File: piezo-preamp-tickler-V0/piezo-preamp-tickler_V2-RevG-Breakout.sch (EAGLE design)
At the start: 67 parts, among them IC1 OPA2134UA, Q1 J201SOT-23, Q2 J201SOT-23, SW2-SPST INPUT-select

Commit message: updated footprints
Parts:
- removed C14: 68uF, SparkFun:CAP_POL3528
- removed SC4503: VREG12_SOT23-5, CMU-ArtFab:VREG12_SOT23-5
- added C11: 10uF, adafruit:C-USC0805K
- added U$1: SC4503, CMU-ArtFab:SC4503
- C13: value 10uF -> 0.1uF; device SparkFun:CAP_POL1206 -> adafruit:C-USC0805K
- C8: value 2.2pf -> 22pF; device SparkFun:CAP_POL1206 -> adafruit:C-USC0805K
- C9: value 56nf -> 10uF; device SparkFun:CAP_POL3528 -> adafruit:C-USC0805K
- U$4, U$5: device CMU-ArtFab:POTTHUMBPOT14MM -> CMU-ArtFab:POTTHUMBPOT14
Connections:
- net +12V: now also C8.1, C9.1; no longer C14.+, C8.+
- net GND: now also C11.2, C13.2, C9.2, U$1.GND; no longer C13.-, C14.-, C9.-, SC4503.GND
- net N$29: now also C13.1, U$1.SHDN; no longer C9.+, SC4503.SHDN
- net N$30: now also C8.2, U$1.FB; no longer C8.-, SC4503.FB
- net N$32: now also U$1.SW; no longer SC4503.SW
- net VBAT: now also C11.1, U$1.IN; no longer C13.+, SC4503.IN
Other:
- moved on the sheet: D7, R18, R9

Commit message: changes to piezo-preamp-tickler_V2-RevG-Breakout -made all names/labels consistent in size/font and readable -moved all parts to top -rearranged (position and rotation) all components to mostly match the layout of the schematic for easier debugging -changed unnecessary 3-pin connectors to 2-pin -added independent 12V power inputs for buffer1 and buffer2 -label all connectors for inputs and outputs to subsystems make buffer1 and 2 identical, with optional caps and resistors -spread out all components as much as possible for easier debugging -added a bypass jumper to buffer to so we can totally disconnect/isolate buffer2 if we just want to list to the opamp output
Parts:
- removed L4: 2.7uH, SparkFun:INDUCTORCR54
- removed PIEZO: (no value), adafruit:JST_2PIN-THM
- removed SW2-SPST: INPUT-select, CMU-ArtFab:SWITCH_SPDTCL-SB-12B
- removed TO-HEADSET, TO-PHONE: AUDIO-JACK3LGPADS, Daniel:AUDIO-JACK3LGPADS
- removed U$2: SWITCH_DPDT, CMU-ArtFab:SWITCH_DPDT
- removed U$4, U$5: (no value), CMU-ArtFab:POTTHUMBPOT14
- added C14: 0.1uF, adafruit:C-USC0805K
- added D5: MMSZ5231B, diode:DIODE-SOD123
- added J10, J11: AUDIO-JACK3LGPADS, Daniel:AUDIO-JACK3LGPADS
- added J12: (no value), SparkFun-Connectors:USB_MICRO-BREDUCED_PASTE
- added J15: Buf2_BYPASS, SparkFun-Connectors:CONN_02
- added J8: OpAmp_OUT, SparkFun-Connectors:CONN_02
- added J9: Buf2_IN, SparkFun-Connectors:CONN_02
- added L1: 2.7 uH, SparkFun-Coils:INDUCTOR-CR54-3.3UH
- added R24: 330, CMU-ArtFab:R-US_R0805
- added R25: 390, CMU-ArtFab:R-US_R0805
- added SW1: SWITCH_DPDT, CMU-ArtFab:SWITCH_DPDT
- added SW2: INPUT-select, CMU-ArtFab:SWITCH_SPDTCL-SB-12B
- added TM1: 20K, adafruit:TRIMPOTTC33X
- C1: value 47uF -> 10uF; device adafruit:C-US -> adafruit:C-USC0805K
- C11: value 10uF -> 0.1uF
- C12: value 0.1uF -> 22pF
- C13: value 0.1uF -> 10uF
- C3: value 10uF -> 150uF; device adafruit:C-USC0805K -> adafruit:C-US
- C4: value 150uF -> 3.3uF
- C6: value 3.3uF -> 10uF; device adafruit:C-US -> adafruit:C-USC0805K
- C7: value 10uF -> 47uF; device adafruit:C-USC0805K -> adafruit:C-US
- C8: value 22pF -> 150uF; device adafruit:C-USC0805K -> adafruit:C-US
- D1: value (none) -> 1N4148; device diode:DIODE-SOD123 -> adafruit:DIODESOD-123; DIGIKEY (none) -> 1N4148WTPMSCT-ND
- D2, D4: value (none) -> MMSZ5231B
- D3: value 1N4148 -> MMSZ5231B; device adafruit:DIODESOD-123 -> diode:DIODE-SOD123; DIGIKEY 1N4148WTPMSCT-ND -> (none)
- J1: value (none) -> 12V; device SparkFun-Connectors:USB_MICRO-BREDUCED_PASTE -> SparkFun-Connectors:CONN_02
- J2, J4: value (none) -> 12V; device SparkFun-Connectors:CONN_03 -> SparkFun-Connectors:CONN_02
- J3: value (none) -> Piezo; device SparkFun-Connectors:CONN_03 -> SparkFun-Connectors:CONN_02
- J5: value (none) -> Buf1_OUT; device SparkFun-Connectors:CONN_03 -> SparkFun-Connectors:CONN_02
- J6: value (none) -> OpAmp_IN
- J7: value (none) -> 12V
- Q1: value J201SOT-23 -> J201
- Q3: value DUAL-NFET-DMN2400 -> DMN2400
- Q4: value BQ21040-LIPO-CHARGER -> BQ21040
- Q6: value BQ297X-BATTERY-MANAGER -> BQ297X
- R1: value 2.2K -> 10; device CMU-ArtFab:R-US_R0603 -> CMU-ArtFab:R-US_R0805
- R10: value 1K -> 10K; device CMU-ArtFab:R-US_R0603 -> CMU-ArtFab:POTTHUMBPOT14
- R11: value 10K -> 1K; device CMU-ArtFab:R-US_R0603 -> CMU-ArtFab:R-US_R0805
- R12: value 390 -> 10K; device CMU-ArtFab:R-US_R0805 -> CMU-ArtFab:POTTHUMBPOT14
- R13: value 10M -> 10K; device CMU-ArtFab:R-US_R0603 -> CMU-ArtFab:R-US_R0805
- R14: value 1.2K -> 1K; device CMU-ArtFab:R-US_R0603 -> CMU-ArtFab:R-US_R0805
- R15: value 1K -> 1M; device CMU-ArtFab:R-US_R0603 -> CMU-ArtFab:R-US_R0805
- R16: value 10 -> 1.2K; device CMU-ArtFab:R-US_R0603 -> CMU-ArtFab:R-US_R0805
- R17: value 10K -> 2.2K; device CMU-ArtFab:R-US_R0603 -> CMU-ArtFab:R-US_R0805
- R18: value 100k -> 10k; device CMU-ArtFab:R-US_R0603 -> CMU-ArtFab:R-US_R0805
- R19, R21: device CMU-ArtFab:R-US_R0603 -> CMU-ArtFab:R-US_R0805
- R2: value 1.2K -> 10M; device CMU-ArtFab:R-US_R0603 -> CMU-ArtFab:R-US_R0805
- R20: value 10k -> 1k; device CMU-ArtFab:R-US_R0603 -> CMU-ArtFab:R-US_R0805
- R22: value 1k -> 866k; device CMU-ArtFab:R-US_R0603 -> CMU-ArtFab:R-US_R0805
- R23: value 330 -> 100k; device CMU-ArtFab:R-US_R0603 -> CMU-ArtFab:R-US_R0805
- R3: value 1M -> 10K; device CMU-ArtFab:R-US_R0603 -> CMU-ArtFab:R-US_R0805
- R4: value 20K -> 1.2K; device adafruit:TRIMPOTTC33X -> CMU-ArtFab:R-US_R0805
- R5: value 100K -> 2.2K; device CMU-ArtFab:R-US_R0603 -> CMU-ArtFab:R-US_R0805
- R6: value 150K -> 1K; device CMU-ArtFab:R-US_R0603 -> CMU-ArtFab:R-US_R0805
- R7: value 1K -> 100K; device CMU-ArtFab:R-US_R0603 -> CMU-ArtFab:R-US_R0805
- R8: value 1K -> 150K; device CMU-ArtFab:R-US_R0603 -> CMU-ArtFab:R-US_R0805
- R9: value 866k -> 1K; device CMU-ArtFab:R-US_R0603 -> CMU-ArtFab:R-US_R0805
- renumbered BATTERY1 to J13, D7 to D6, POWER to SW3, U$1 to Q5, U$10 to Q6, U$13 to Q4, U$14 to Q3
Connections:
- removed net N$47: C3.2, IC1A.V-, J3.1, J4.1, R6.1
- new net N$20: C3.2, D3.C, J3.1, J4.1, J5.1, R2.1, R4.1, R5.1
- new net N$46: J15.2, R13.2, R14.2
- new net N$8: D2.A, D3.A
- net +12V: now also C12.1, C13.1, D1.A, R22.2; no longer C8.1, C9.1, D3.A, R9.2
- net GND: now also C1.2, J1.1, J2.1, LED2.C, R23.1; no longer C5.2, J7.1, LED1.C, R18.1
- net GND1: now also C14.2, J12.GND, R18.1; no longer C12.2, J1.GND, R20.1
- net N$1: now also D4.A, D5.A; no longer D1.A, D2.A
- net N$10: now also D4.C, R14.1, R15.2; no longer D1.C, R10.1, R3.2
- net N$11: now also J15.1, J9.2, SW1.P$1, SW1.P$4; no longer J5.2, R10.2, R17.2, U$2.P$1, U$2.P$4
- net N$12: now also J10.EARTH, SW2.1; no longer SW2-SPST.1, TO-HEADSET.EARTH
- net N$13: now also J10.TIP, SW1.P$2; no longer TO-HEADSET.TIP, U$2.P$2
- net N$14: now also C3.1, R4.2; no longer C4.1, R14.2
- net N$15: now also J10.RING1, SW1.P$5; no longer TO-HEADSET.RING1, U$2.P$5
- net N$16: now also C1.1, D1.C, R1.2; no longer C5.1, D3.C, R16.2
- net N$17: now also J11.EARTH, SW2.2; no longer SW2-SPST.2, TO-PHONE.EARTH
- net N$18: now also LED2.A, R25.1; no longer LED1.A, R12.1
- net N$19: now also J6.2, TM1.E; no longer J4.2, R4.E
- net N$2: now also D2.C, J3.2, R2.2; no longer D4.C, PIEZO.1, R13.2
- net N$22: now also R6.1; no longer R15.1
- net N$23: now also C5.1, R11.2, R7.1, R8.2; no longer C3.1, R15.2, R5.1, R7.2
- net N$24: now also R9.1, TM1.S; no longer R4.S, R8.1
- net N$25: now also J4.2, R3.2; no longer J2.3, R11.2
- net N$26: now also J11.RING1, SW1.P$6; no longer TO-PHONE.RING1, U$2.P$6
- net N$27: now also J11.TIP, SW1.P$3; no longer TO-PHONE.TIP, U$2.P$3
- net N$28: now also C4.2, J5.2; no longer C6.2, J2.2
- net N$29: now also C11.1; no longer C13.1
- net N$3: now also C8.1, R16.2; no longer R2.2
- net N$30: now also C12.2, R22.1, R23.2; no longer C8.2, R18.2, R9.1
- net N$31: now also C6.1, R12.WIPER; no longer C7.1, U$5.WIPER
- net N$32: now also L1.2; no longer L4.2
- net N$33: now also R20.2; no longer R22.2
- net N$34: now also C14.1, R24.2; no longer C12.1, R23.2
- net N$35: now also R21.2; no longer R20.2
- net N$36: now also C7.2, J8.2; no longer C1.2, J3.2
- net N$38: now also R18.2; no longer R21.2
- net N$40: now also LED1.C, R20.1; no longer LED2.C, R22.1
- net N$42: now also J7.2, R7.2; no longer J4.3, R5.2
- net N$43: now also J1.2, J2.2, R1.1; no longer J6.2, J7.2, R16.1
- net N$44: now also C5.2, IC1A.V-, J6.1, J7.1, J8.1, R8.1; no longer C4.2, D4.A, J2.1, PIEZO.2, R13.1, R14.1
- net N$45: now also C8.2, D5.C, J10.RING2, J11.RING2, J9.1, R13.1, R15.1, R16.1; no longer D2.C, J5.1, R1.1, R2.1, R3.1, TO-HEADSET.RING2, TO-PHONE.RING2
- net N$5: now also R11.1; no longer R7.1
- net N$6: now also C6.2, C7.1, R10.WIPER; no longer C1.1, C7.2, U$4.WIPER
- net N$7: now also R10.IN, R12.IN, R9.2; no longer R8.2, U$4.IN, U$5.IN
- net N$9: now also C4.1, R3.1, R5.2; no longer C6.1, R11.1
- net SELECT: now also R17.2, SW2.3; no longer R1.2, SW2-SPST.3
- net V+: now also J12.VBUS, LED1.A; no longer J1.VBUS, LED2.A
- net VBAT: now also C9.1, L1.1, R24.1, R25.2; no longer C11.1, L4.1, R12.2, R23.1
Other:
- moved on the sheet: C1, C11, C12, C13, C2, C3, C4, C5, C6, C7, C9, D1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

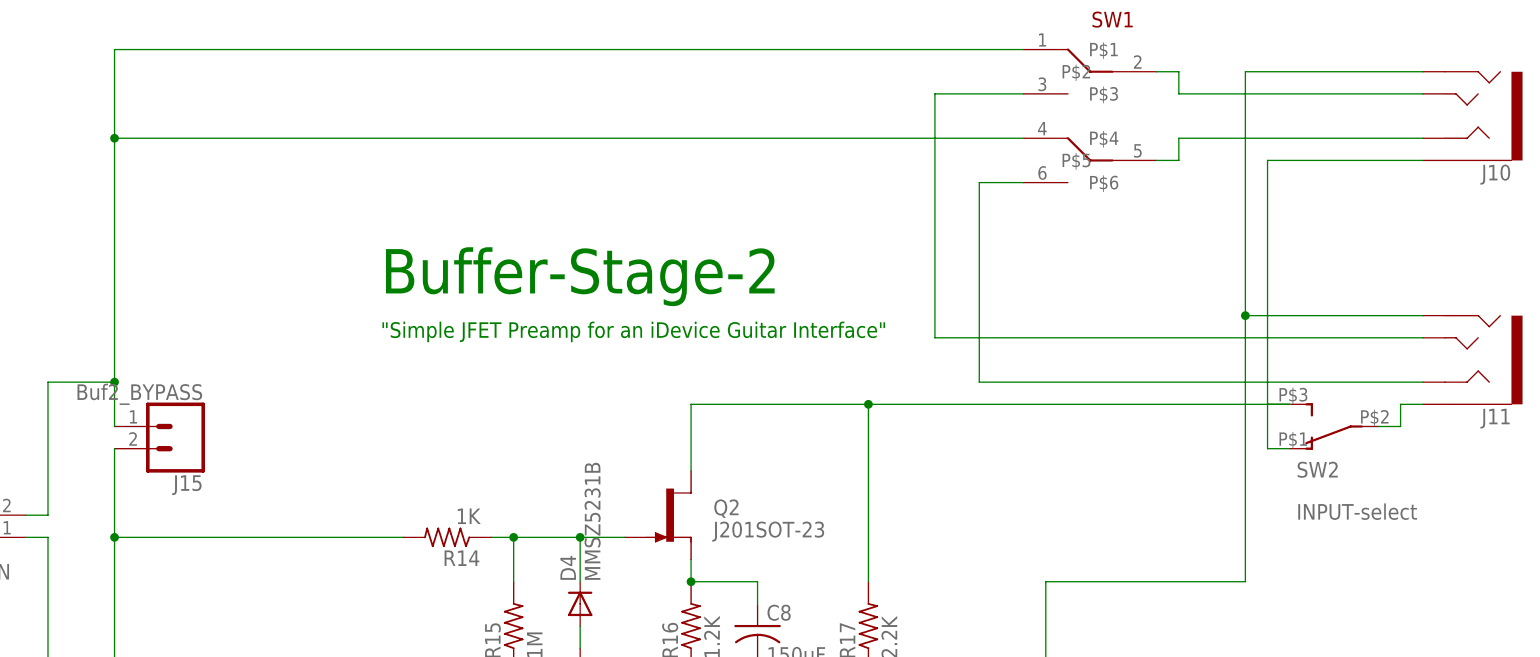
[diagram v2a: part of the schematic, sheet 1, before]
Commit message: renumbered parts in piezo-preamp-tickler_V2-RevG-Breakout
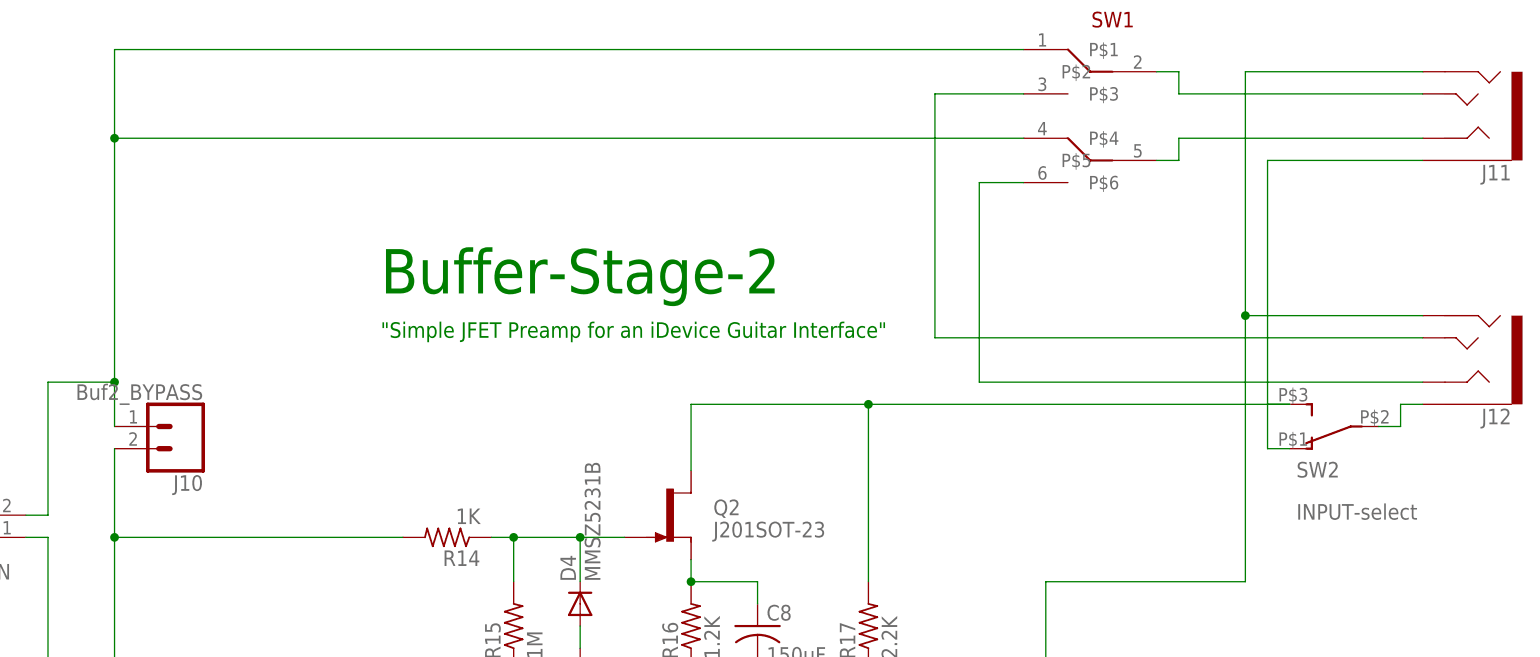
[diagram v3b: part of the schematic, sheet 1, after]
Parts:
- removed J15: Buf2_BYPASS, SparkFun-Connectors:CONN_02
- added J14: (no value), SparkFun-Connectors:CONN_02LOCK
- J10: value AUDIO-JACK3LGPADS -> Buf2_BYPASS; device Daniel:AUDIO-JACK3LGPADS -> SparkFun-Connectors:CONN_02
- J12: value (none) -> AUDIO-JACK3LGPADS; device SparkFun-Connectors:USB_MICRO-BREDUCED_PASTE -> Daniel:AUDIO-JACK3LGPADS
- J13: device SparkFun-Connectors:CONN_02LOCK -> SparkFun-Connectors:USB_MICRO-BREDUCED_PASTE
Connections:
- net GND1: now also J13.GND; no longer J12.GND
- net N$11: now also J10.1; no longer J15.1
- net N$12: now also J11.EARTH; no longer J10.EARTH
- net N$13: now also J11.TIP; no longer J10.TIP
- net N$15: now also J11.RING1; no longer J10.RING1
- net N$17: now also J12.EARTH; no longer J11.EARTH
- net N$21: now also J14.2; no longer J13.2
- net N$26: now also J12.RING1; no longer J11.RING1
- net N$27: now also J12.TIP; no longer J11.TIP
- net N$45: now also J12.RING2; no longer J10.RING2
- net N$46: now also J10.2; no longer J15.2
- net V+: now also J13.VBUS; no longer J12.VBUS
- net VBAT: now also J14.1; no longer J13.1
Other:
- moved on the sheet: J11
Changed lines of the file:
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@@
 <part name="R15" library="CMU-ArtFab" deviceset="R-US_" device="R0805" value="1M"/>
 <part name="R14" library="CMU-ArtFab" deviceset="R-US_" device="R0805" value="1K"/>
+<part name="J12" library="Daniel" deviceset="AUDIO-JACK3" device="LGPADS"/>
 <part name="J11" library="Daniel" deviceset="AUDIO-JACK3" device="LGPADS"/>
-<part name="J10" library="Daniel" deviceset="AUDIO-JACK3" device="LGPADS"/>
 <part name="IC1" library="linear" library_urn="urn:adsk.eagle:library:262" deviceset="OPA2*" device="UA" technology="134" value="OPA2134UA"/>
 <part name="LED2" library="led" library_urn="urn:adsk.eagle:library:259" deviceset="LED" device="3MM"/>
@@
 <part name="U5" library="microbuilder" deviceset="VBAT" device=""/>
 <part name="SW3" library="CMU-ArtFab" deviceset="SWITCH_SPDT" device="CL-SB-12B" value="SPDT"/>
-<part name="J13" library="SparkFun-Connectors" deviceset="CONN_02" device="LOCK"/>
+<part name="J14" library="SparkFun-Connectors" deviceset="CONN_02" device="LOCK"/>
 <part name="D4" library="diode" library_urn="urn:adsk.eagle:library:210" deviceset="DIODE-" device="SOD123" value="MMSZ5231B"/>
 <part name="D5" library="diode" library_urn="urn:adsk.eagle:library:210" deviceset="DIODE-" device="SOD123" value="MMSZ5231B"/>
@@
 <part name="GND4" library="SparkFun" deviceset="GND" device=""/>
 <part name="P+4" library="supply1" library_urn="urn:adsk.eagle:library:371" deviceset="+12V" device=""/>
-<part name="J12" library="SparkFun-Connectors" library_urn="urn:adsk.eagle:library:513" deviceset="USB_MICRO-B" device="REDUCED_PASTE"/>
+<part name="J13" library="SparkFun-Connectors" library_urn="urn:adsk.eagle:library:513" deviceset="USB_MICRO-B" device="REDUCED_PASTE"/>
 <part name="LED1" library="led" library_urn="urn:adsk.eagle:library:259" deviceset="LED" device="3MM"/>
 <part name="U2" library="microbuilder" deviceset="VBAT" device=""/>
@@
 <part name="R5" library="CMU-ArtFab" deviceset="R-US_" device="R0805" value="2.2K"/>
 <part name="C8" library="adafruit" deviceset="C-US" device="" value="150uF"/>
-<part name="J15" library="SparkFun-Connectors" library_urn="urn:adsk.eagle:library:513" deviceset="CONN_02" device="" value="Buf2_BYPASS"/>
+<part name="J10" library="SparkFun-Connectors" library_urn="urn:adsk.eagle:library:513" deviceset="CONN_02" device="" value="Buf2_BYPASS"/>
 </parts>
 <sheets>
@@
 <instance part="R15" gate="G$1" x="182.88" y="20.32" rot="R90"/>
 <instance part="R14" gate="G$1" x="175.26" y="30.48" rot="R180"/>
-<instance part="J11" gate="G$1" x="292.1" y="50.8" smashed="yes" rot="R180">
+<instance part="J12" gate="G$1" x="292.1" y="50.8" smashed="yes" rot="R180">
 <attribute name="NAME" x="297.18" y="45.212" size="1.778" layer="95" rot="R180"/>
 </instance>
-<instance part="J10" gate="G$1" x="292.1" y="78.74" smashed="yes" rot="R180">
+<instance part="J11" gate="G$1" x="292.1" y="78.74" smashed="yes" rot="R180">
 <attribute name="NAME" x="297.18" y="73.152" size="1.778" layer="95" rot="R180"/>
 </instance>
@@
 <instance part="R5" gate="G$1" x="-38.1" y="27.94" rot="R90"/>
 <instance part="C8" gate="G$1" x="210.82" y="20.32"/>
-<instance part="J15" gate="G$1" x="144.78" y="43.18" rot="R180"/>
+<instance part="J10" gate="G$1" x="144.78" y="43.18" rot="R180"/>
 </instances>
 <busses>
@@
 <wire x1="129.54" y1="33.02" x2="129.54" y2="48.26" width="0.1524" layer="91"/>
 <wire x1="129.54" y1="48.26" x2="137.16" y2="48.26" width="0.1524" layer="91"/>
-<pinref part="J15" gate="G$1" pin="1"/>
+<pinref part="J10" gate="G$1" pin="1"/>
 <wire x1="137.16" y1="48.26" x2="137.16" y2="43.18" width="0.1524" layer="91"/>
 <junction x="137.16" y="48.26"/>
@@
 <net name="N$12" class="0">
 <segment>
-<pinref part="J10" gate="G$1" pin="EARTH"/>
+<pinref part="J11" gate="G$1" pin="EARTH"/>
 <wire x1="287.02" y1="73.66" x2="269.24" y2="73.66" width="0.1524" layer="91"/>
 <wire x1="269.24" y1="73.66" x2="269.24" y2="40.64" width="0.1524" layer="91"/>
@@
 <net name="N$13" class="0">
 <segment>
-<pinref part="J10" gate="G$1" pin="TIP"/>
+<pinref part="J11" gate="G$1" pin="TIP"/>
 <wire x1="287.02" y1="81.28" x2="259.08" y2="81.28" width="0.1524" layer="91"/>
 <wire x1="259.08" y1="81.28" x2="259.08" y2="83.82" width="0.1524" layer="91"/>
@@
 <net name="N$15" class="0">
 <segment>
-<pinref part="J10" gate="G$1" pin="RING1"/>
+<pinref part="J11" gate="G$1" pin="RING1"/>
 <wire x1="259.08" y1="76.2" x2="287.02" y2="76.2" width="0.1524" layer="91"/>
 <wire x1="259.08" y1="76.2" x2="259.08" y2="73.66" width="0.1524" layer="91"/>
@@
 <net name="N$17" class="0">
 <segment>
-<pinref part="J11" gate="G$1" pin="EARTH"/>
+<pinref part="J12" gate="G$1" pin="EARTH"/>
 <wire x1="287.02" y1="45.72" x2="284.48" y2="45.72" width="0.1524" layer="91"/>
 <wire x1="284.48" y1="45.72" x2="284.48" y2="43.18" width="0.1524" layer="91"/>
@@
 <net name="N$26" class="0">
 <segment>
-<pinref part="J11" gate="G$1" pin="RING1"/>
+<pinref part="J12" gate="G$1" pin="RING1"/>
 <wire x1="287.02" y1="48.26" x2="236.22" y2="48.26" width="0.1524" layer="91"/>
 <wire x1="236.22" y1="48.26" x2="236.22" y2="71.12" width="0.1524" layer="91"/>
@@
 <net name="N$27" class="0">
 <segment>
-<pinref part="J11" gate="G$1" pin="TIP"/>
+<pinref part="J12" gate="G$1" pin="TIP"/>
 <wire x1="287.02" y1="53.34" x2="231.14" y2="53.34" width="0.1524" layer="91"/>
 <wire x1="231.14" y1="53.34" x2="231.14" y2="81.28" width="0.1524" layer="91"/>
@@
 <pinref part="D5" gate="G$1" pin="C"/>
 <wire x1="266.7" y1="55.88" x2="266.7" y2="25.4" width="0.1524" layer="91"/>
-<pinref part="J11" gate="G$1" pin="RING2"/>
+<pinref part="J12" gate="G$1" pin="RING2"/>
 <wire x1="287.02" y1="55.88" x2="266.7" y2="55.88" width="0.1524" layer="91"/>
 <wire x1="266.7" y1="55.88" x2="266.7" y2="83.82" width="0.1524" layer="91"/>
 <junction x="266.7" y="55.88"/>
-<pinref part="J10" gate="G$1" pin="RING2"/>
+<pinref part="J11" gate="G$1" pin="RING2"/>
 <wire x1="266.7" y1="83.82" x2="287.02" y2="83.82" width="0.1524" layer="91"/>
 <wire x1="266.7" y1="25.4" x2="243.84" y2="25.4" width="0.1524" layer="91"/>
@@
 <wire x1="137.16" y1="30.48" x2="170.18" y2="30.48" width="0.1524" layer="91"/>
 <wire x1="137.16" y1="30.48" x2="137.16" y2="15.24" width="0.1524" layer="91"/>
-<pinref part="J15" gate="G$1" pin="2"/>
+<pinref part="J10" gate="G$1" pin="2"/>
 <wire x1="137.16" y1="40.64" x2="137.16" y2="30.48" width="0.1524" layer="91"/>
 <junction x="137.16" y="30.48"/>
@@
 <instance part="U5" gate="G$1" x="195.58" y="172.72"/>
 <instance part="SW3" gate="G$1" x="203.2" y="157.48"/>
-<instance part="J13" gate="G$1" x="220.98" y="162.56" rot="R180"/>
+<instance part="J14" gate="G$1" x="220.98" y="162.56" rot="R180"/>
 <instance part="U1" gate="G$1" x="63.5" y="71.12"/>
 <instance part="D6" gate="G$1" x="134.62" y="66.04" smashed="yes">
@@
 <instance part="GND4" gate="1" x="129.54" y="48.26"/>
 <instance part="P+4" gate="1" x="170.18" y="71.12"/>
-<instance part="J12" gate="G$1" x="53.34" y="165.1" rot="MR0"/>
+<instance part="J13" gate="G$1" x="53.34" y="165.1" rot="MR0"/>
 <instance part="LED1" gate="G$1" x="134.62" y="160.02"/>
 <instance part="U2" gate="G$1" x="119.38" y="160.02" rot="R270"/>
@@
 <wire x1="195.58" y1="162.56" x2="195.58" y2="170.18" width="0.1524" layer="91"/>
 <wire x1="195.58" y1="162.56" x2="213.36" y2="162.56" width="0.1524" layer="91"/>
-<pinref part="J13" gate="G$1" pin="1"/>
+<pinref part="J14" gate="G$1" pin="1"/>
 </segment>
 <segment>
@@
 <pinref part="SW3" gate="G$1" pin="1"/>
 <wire x1="208.28" y1="160.02" x2="213.36" y2="160.02" width="0.1524" layer="91"/>
-<pinref part="J13" gate="G$1" pin="2"/>
+<pinref part="J14" gate="G$1" pin="2"/>
 </segment>
 </net>
@@
 <pinref part="P+2" gate="1" pin="V+"/>
 <wire x1="63.5" y1="172.72" x2="63.5" y2="170.18" width="0.1524" layer="91"/>
-<pinref part="J12" gate="G$1" pin="VBUS"/>
+<pinref part="J13" gate="G$1" pin="VBUS"/>
 <wire x1="63.5" y1="170.18" x2="58.42" y2="170.18" width="0.1524" layer="91"/>
 <pinref part="Q4" gate="G$1" pin="VIN"/>
@@
 <junction x="66.04" y="162.56"/>
 <pinref part="Q4" gate="G$1" pin="GND"/>
-<pinref part="J12" gate="G$1" pin="GND"/>
+<pinref part="J13" gate="G$1" pin="GND"/>
 <wire x1="71.12" y1="160.02" x2="66.04" y2="160.02" width="0.1524" layer="91"/>
 <pinref part="R18" gate="G$1" pin="1"/>

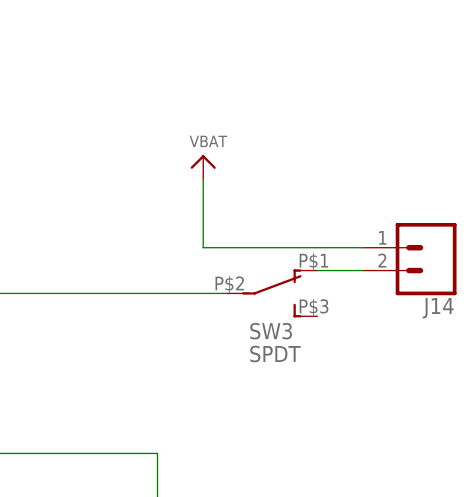
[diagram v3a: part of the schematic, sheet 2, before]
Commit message: renumbered parts in piezo-preamp-tickler_V2-RevG-Breakout
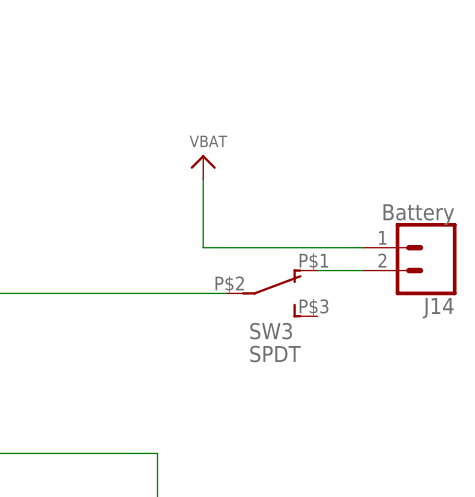
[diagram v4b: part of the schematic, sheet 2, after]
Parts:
- J14: value (none) -> Battery
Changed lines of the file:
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@@
 <part name="U5" library="microbuilder" deviceset="VBAT" device=""/>
 <part name="SW3" library="CMU-ArtFab" deviceset="SWITCH_SPDT" device="CL-SB-12B" value="SPDT"/>
-<part name="J14" library="SparkFun-Connectors" deviceset="CONN_02" device="LOCK"/>
+<part name="J14" library="SparkFun-Connectors" deviceset="CONN_02" device="LOCK" value="Battery"/>
 <part name="D4" library="diode" library_urn="urn:adsk.eagle:library:210" deviceset="DIODE-" device="SOD123" value="MMSZ5231B"/>
 <part name="D5" library="diode" library_urn="urn:adsk.eagle:library:210" deviceset="DIODE-" device="SOD123" value="MMSZ5231B"/>
